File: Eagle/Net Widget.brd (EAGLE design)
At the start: 76.2 x 45.7 mm, 14 parts, among them IC1 ATmega1284P

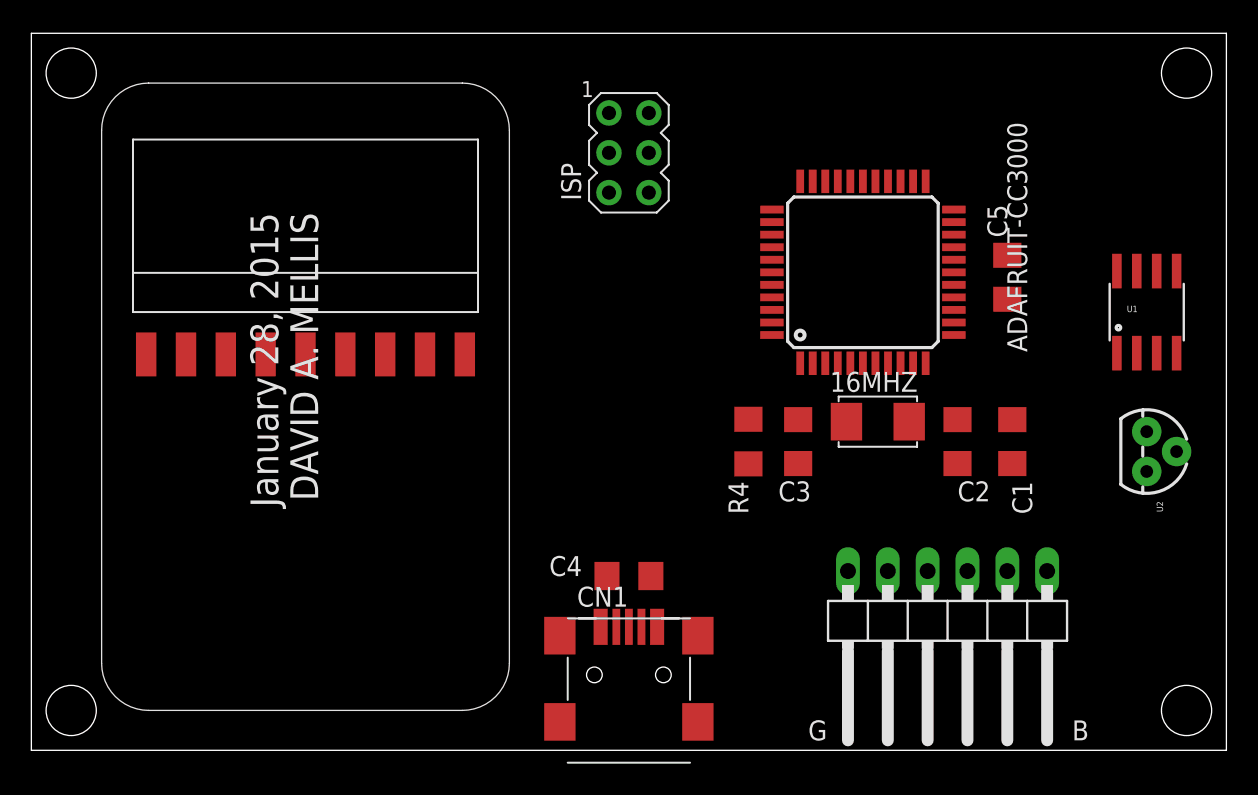
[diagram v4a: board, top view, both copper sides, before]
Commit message: Match CS and VBEN to Wicked Devices wildfire.
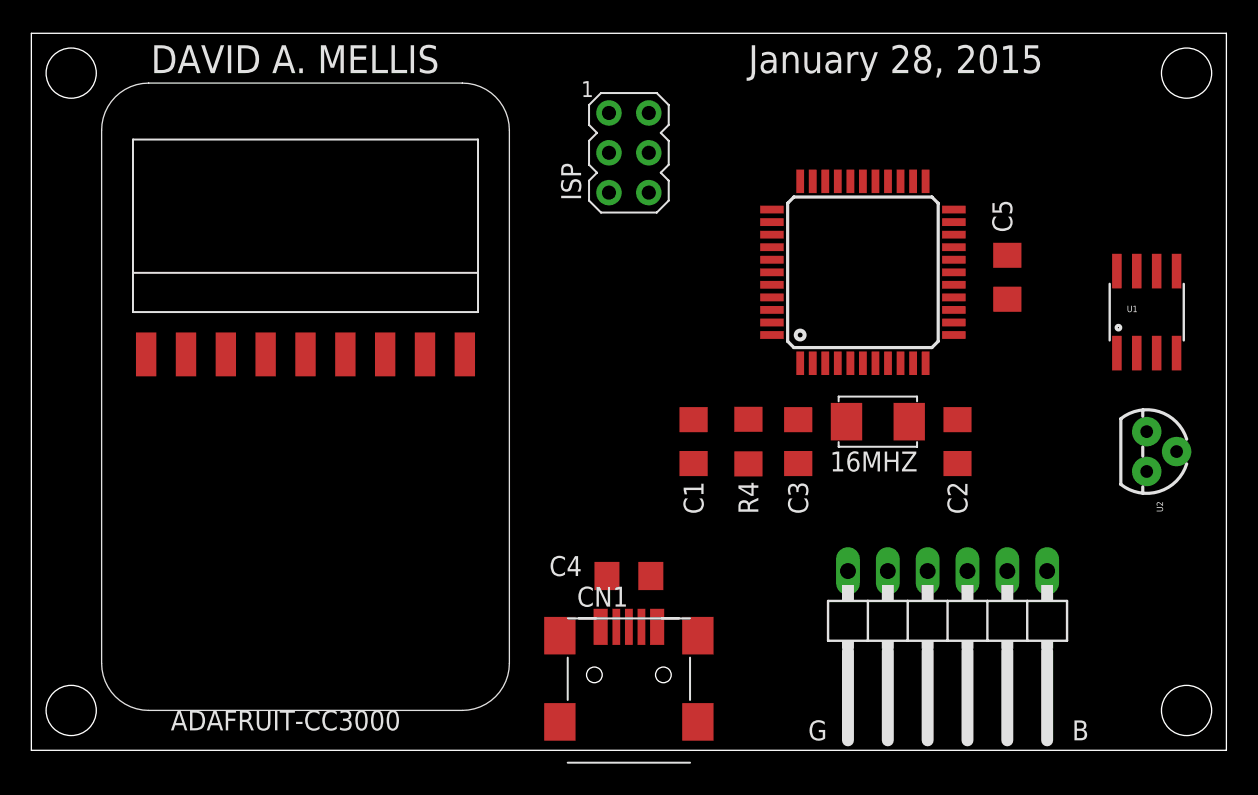
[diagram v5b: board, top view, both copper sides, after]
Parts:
- moved C1 20.3 mm to (42.2, 19.7)
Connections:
- net CS: now also IC1.40; no longer IC1.22
- net VBEN: now also IC1.41; no longer IC1.23
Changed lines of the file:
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@@
 <layer number="39" name="tKeepout" color="4" fill="11" visible="no" active="yes"/>
 <layer number="40" name="bKeepout" color="1" fill="11" visible="no" active="yes"/>
-<layer number="41" name="tRestrict" color="4" fill="10" visible="no" active="yes"/>
-<layer number="42" name="bRestrict" color="1" fill="10" visible="no" active="yes"/>
+<layer number="41" name="tRestrict" color="4" fill="10" visible="yes" active="yes"/>
+<layer number="42" name="bRestrict" color="1" fill="10" visible="yes" active="yes"/>
 <layer number="43" name="vRestrict" color="2" fill="10" visible="no" active="yes"/>
 <layer number="44" name="Drills" color="7" fill="1" visible="yes" active="yes"/>
@@
 <hole x="2.54" y="43.18" drill="3.2"/>
 <hole x="2.54" y="2.54" drill="3.2"/>
-<polygon width="0.4064" layer="41">
-<vertex x="37.465" y="20.32"/>
-<vertex x="38.735" y="20.32"/>
-<vertex x="41.275" y="22.86"/>
-<vertex x="41.275" y="25.4"/>
-<vertex x="46.355" y="25.4"/>
-<vertex x="46.355" y="24.13"/>
-<vertex x="44.45" y="24.13"/>
-<vertex x="44.45" y="15.24"/>
-<vertex x="46.355" y="15.24"/>
-<vertex x="46.355" y="13.97"/>
-<vertex x="41.275" y="13.97"/>
-<vertex x="41.275" y="16.51"/>
-<vertex x="39.37" y="18.415"/>
-<vertex x="37.465" y="18.415"/>
-</polygon>
-<text x="63.5" y="25.4" size="1.27" layer="25" font="fixed" rot="R90">ADAFRUIT-CC3000</text>
-<text x="16.51" y="34.29" size="1.778" layer="25" font="fixed" rot="R270">DAVID A. MELLIS</text>
-<text x="13.97" y="34.29" size="1.778" layer="25" font="fixed" rot="R270">January 28, 2015</text>
+<text x="8.89" y="1.27" size="1.27" layer="25" font="fixed">ADAFRUIT-CC3000</text>
+<text x="7.62" y="43.18" size="1.778" layer="25" font="fixed">DAVID A. MELLIS</text>
+<text x="45.72" y="43.18" size="1.778" layer="25" font="fixed">January 28, 2015</text>
 <text x="66.3575" y="0.635" size="1.27" layer="25" font="fixed" rot="SR0">B</text>
 <text x="49.53" y="0.635" size="1.27" layer="25" font="fixed" rot="SR0">G</text>
+<polygon width="0.4064" layer="42">
+<vertex x="48.26" y="17.78"/>
+<vertex x="59.69" y="17.78"/>
+<vertex x="59.69" y="22.86"/>
+<vertex x="54.61" y="22.86"/>
+<vertex x="54.61" y="25.4"/>
+<vertex x="53.6575" y="25.4"/>
+<vertex x="53.6575" y="22.86"/>
+<vertex x="48.26" y="22.86"/>
+</polygon>
 </plain>
 <attributes>
@@
 <elements>
 <element name="C2" library="rcl" package="C1206" value="18pF" x="59.055" y="19.685" smashed="yes" rot="R90">
-<attribute name="NAME" x="59.055" y="15.875" size="1.27" layer="25" font="fixed"/>
-<attribute name="VALUE" x="57.785" y="14.605" size="1.27" layer="27" font="fixed" rot="R90"/>
+<attribute name="NAME" x="58.42" y="17.145" size="1.27" layer="25" font="fixed" rot="R270"/>
+<attribute name="VALUE" x="61.2775" y="17.4625" size="1.27" layer="27" font="fixed" rot="R90"/>
 </element>
 <element name="C3" library="rcl" package="C1206" value="18pF" x="48.895" y="19.685" smashed="yes" rot="R90">
-<attribute name="NAME" x="47.625" y="15.875" size="1.27" layer="25" font="fixed"/>
-<attribute name="VALUE" x="51.435" y="14.605" size="1.27" layer="27" font="fixed" rot="R90"/>
+<attribute name="NAME" x="48.26" y="17.145" size="1.27" layer="25" font="fixed" rot="R270"/>
+<attribute name="VALUE" x="47.9425" y="17.4625" size="1.27" layer="27" font="fixed" rot="R90"/>
 </element>
 <element name="ISP" library="adafruit" package="AVRISP" value="AVRISP-6" x="38.1" y="38.1" smashed="yes">
@@
 </element>
 <element name="C5" library="rcl" package="C1206" value="0.1uF" x="62.23" y="30.1625" smashed="yes" rot="R90">
-<attribute name="NAME" x="62.23" y="32.7025" size="1.27" layer="25" font="fixed" rot="R90"/>
-<attribute name="VALUE" x="64.77" y="28.8925" size="1.27" layer="27" font="fixed" rot="R90"/>
+<attribute name="NAME" x="62.5475" y="33.02" size="1.27" layer="25" font="fixed" rot="R90"/>
+<attribute name="VALUE" x="64.4525" y="27.6225" size="1.27" layer="27" font="fixed" rot="R90"/>
 </element>
 <element name="16MHZ" library="Net Widget" package="2-SMD-5X3MM" value="CRYSTAL" x="53.975" y="20.955" smashed="yes" rot="R180">
-<attribute name="NAME" x="56.515" y="24.13" size="1.27" layer="25" font="fixed" rot="R180"/>
+<attribute name="NAME" x="56.515" y="19.05" size="1.27" layer="25" font="fixed" rot="R180"/>
 </element>
 <element name="R4" library="rcl" package="R1206" value="10K" x="45.72" y="19.685" smashed="yes" rot="R270">
-<attribute name="NAME" x="44.45" y="17.145" size="1.27" layer="25" rot="R270"/>
-<attribute name="VALUE" x="43.18" y="20.955" size="1.27" layer="27" rot="R270"/>
+<attribute name="NAME" x="45.085" y="17.145" size="1.27" layer="25" rot="R270"/>
+<attribute name="VALUE" x="43.4975" y="20.955" size="1.27" layer="27" rot="R270"/>
 </element>
 <element name="IC1" library="avr-5" package="TQFP44" value="ATmega1284P" x="53.0225" y="30.48" smashed="yes" rot="R90">
-<attribute name="VALUE" x="45.9026" y="25.0825" size="1.778" layer="27" rot="R90"/>
+<attribute name="VALUE" x="62.5475" y="39.5526" size="1.778" layer="27" rot="R180"/>
 </element>
 <element name="JP5" library="Net Widget" package="1X06/90" value="FTDI" x="58.42" y="7.62" smashed="yes" rot="R180">
 <attribute name="VALUE" x="66.675" y="8.89" size="1.27" layer="27" rot="SR270"/>
 </element>
-<element name="C1" library="rcl" package="C1206" value="0.1uF" x="62.5475" y="19.685" smashed="yes" rot="R270">
-<attribute name="NAME" x="62.5475" y="17.145" size="1.27" layer="25" rot="R270"/>
-<attribute name="VALUE" x="63.8175" y="22.225" size="1.27" layer="27" rot="R270"/>
+<element name="C1" library="rcl" package="C1206" value="0.1uF" x="42.2275" y="19.685" smashed="yes" rot="R270">
+<attribute name="NAME" x="41.5925" y="17.145" size="1.27" layer="25" rot="R270"/>
+<attribute name="VALUE" x="39.6875" y="22.225" size="1.27" layer="27" rot="R270"/>
 </element>
 <element name="CN1" library="Net Widget" package="USB-MINIB-POWER" value="" x="38.1" y="2.54"/>
@@
 <contactref element="R4" pad="1"/>
 <contactref element="C1" pad="1"/>
-<wire x1="51.4225" y1="24.68" x2="62.5475" y2="21.085" width="0" layer="19" extent="1-1"/>
 <wire x1="45.72" y1="21.107" x2="51.4225" y2="24.68" width="0" layer="19" extent="1-1"/>
-<wire x1="36.83" y1="35.56" x2="45.72" y2="21.107" width="0" layer="19" extent="1-1"/>
+<wire x1="42.2275" y1="21.085" x2="45.72" y2="21.107" width="0" layer="19" extent="1-1"/>
+<wire x1="36.83" y1="35.56" x2="42.2275" y2="21.085" width="0" layer="19" extent="1-1"/>
 </signal>
 <signal name="MOSI">
@@
 <signal name="CS">
 <contactref element="U$2" pad="P$7"/>
-<contactref element="IC1" pad="22"/>
-<wire x1="12.4" y1="25.245" x2="58.8225" y2="34.48" width="0" layer="19" extent="1-1"/>
+<contactref element="IC1" pad="40"/>
+<wire x1="12.4" y1="25.245" x2="47.2225" y2="29.68" width="0" layer="19" extent="1-1"/>
 </signal>
 <signal name="VBEN">
 <contactref element="U$2" pad="P$8"/>
-<contactref element="IC1" pad="23"/>
-<wire x1="9.86" y1="25.245" x2="57.0225" y2="36.28" width="0" layer="19" extent="1-1"/>
+<contactref element="IC1" pad="41"/>
+<wire x1="9.86" y1="25.245" x2="47.2225" y2="28.88" width="0" layer="19" extent="1-1"/>
 </signal>
 <signal name="IRQ">
@@
 <contactref element="JP5" pad="6"/>
 <contactref element="C1" pad="2"/>
-<wire x1="52.07" y1="11.43" x2="62.5475" y2="18.285" width="0" layer="19" extent="1-1"/>
+<wire x1="42.2275" y1="18.285" x2="52.07" y2="11.43" width="0" layer="19" extent="1-1"/>
 </signal>
 <signal name="RX">

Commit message: Auto-route board.
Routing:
- net VCC: track 0.00 -> 150.6 mm, vias 0 -> 3
- net GND: track 0.00 -> 141.6 mm, vias 0 -> 1
- net MOSI: track 0.00 -> 58.8 mm, vias 0 -> 1
- net MISO: track 0.00 -> 52.9 mm, vias 0 -> 2
- net SCK: track 0.00 -> 49.5 mm, vias 0 -> 2
- net CS: track 0.00 -> 43.2 mm
- net IRQ: track 0.00 -> 41.5 mm, vias 0 -> 2
- net VBEN: track 0.00 -> 39.7 mm, vias 0 -> 2
- net N$2: track 0.00 -> 32.3 mm, vias 0 -> 1
- net RESET: track 0.00 -> 27.9 mm
- net TX: track 0.00 -> 25.5 mm, vias 0 -> 1
- net N$1: track 0.00 -> 24.8 mm
- net RX: track 0.00 -> 18.4 mm
- net DTR: track 0.00 -> 12.7 mm
- net N$6: track 0.00 -> 7.64 mm
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
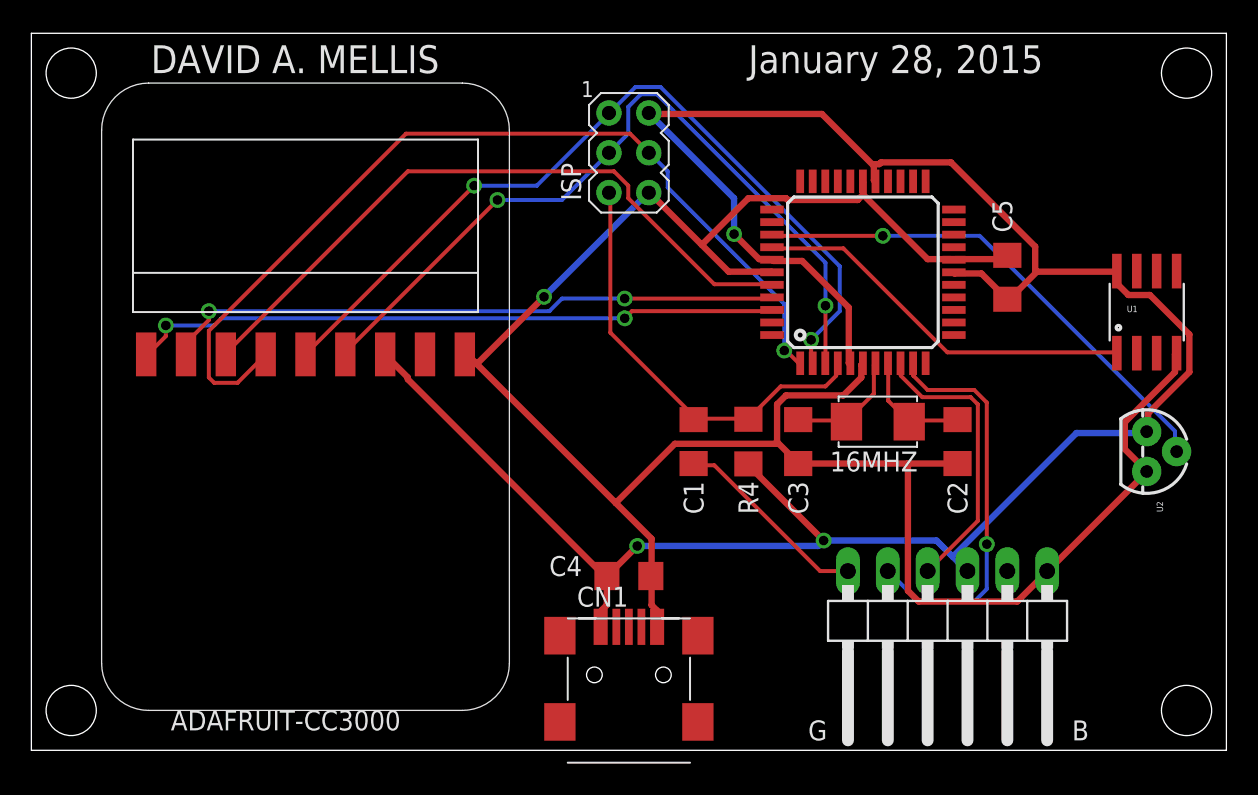
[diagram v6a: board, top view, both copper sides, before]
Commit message: Re-route w/ more space between pads and vias.
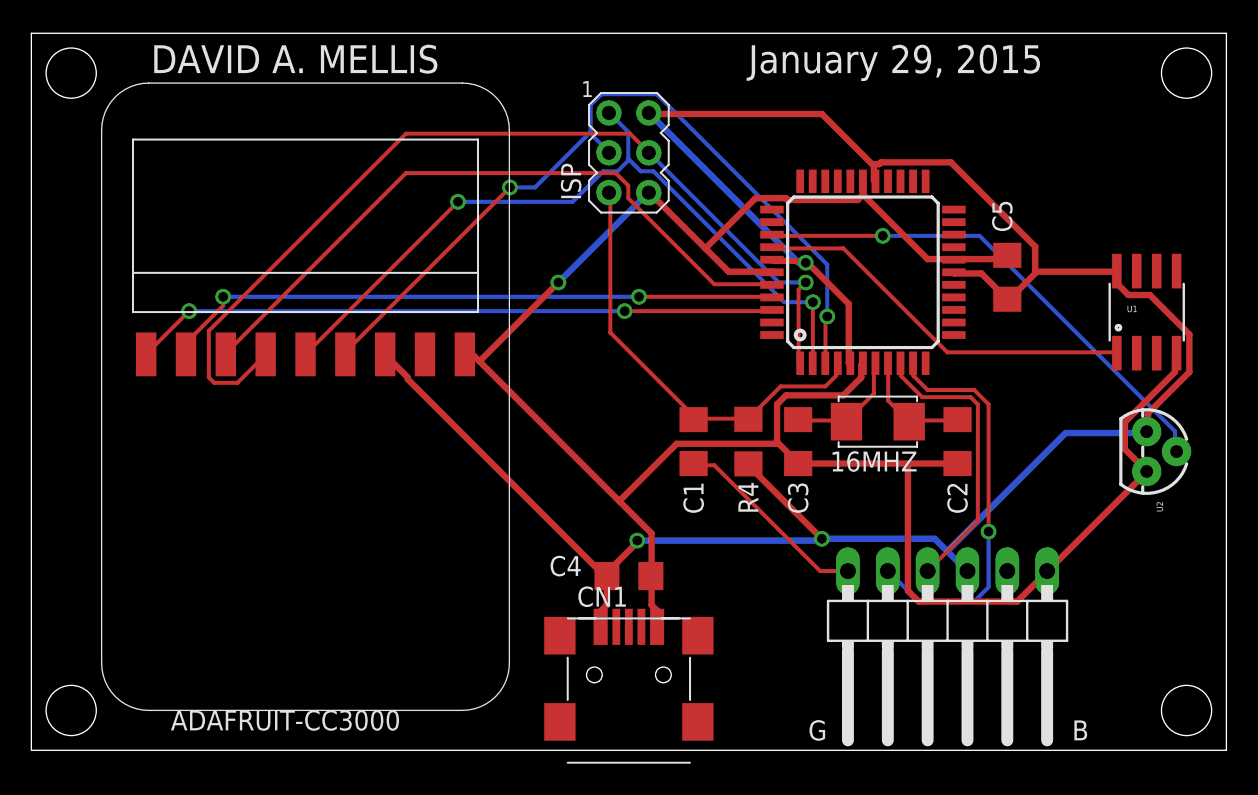
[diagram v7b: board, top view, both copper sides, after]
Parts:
- U1, U2: value (none) -> TMP36
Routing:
- net MISO: track 52.9 -> 48.7 mm
- net SCK: track 49.5 -> 51.3 mm
- net VCC: track 150.6 -> 152.1 mm
- net MOSI: track 58.8 -> 60.1 mm
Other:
- board text added: "January 29, 2015"
- board text removed: "January 28, 2015"

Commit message: Remove temp sensor; add LEDs and touch.
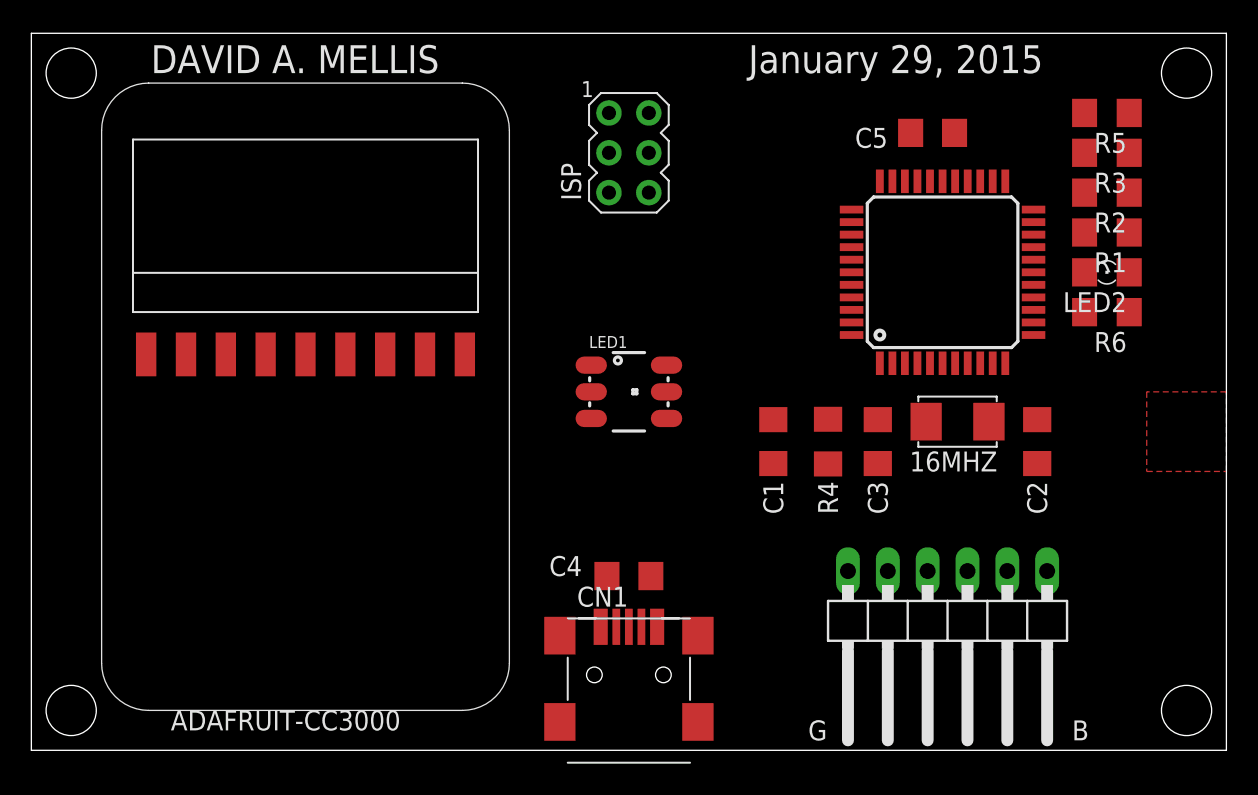
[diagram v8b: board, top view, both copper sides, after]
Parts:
- removed U1: TMP36, Net Widget:SO08
- removed U2: TMP36, Net Widget:TO-92
- added LED1: LED-TRICOLOR-5050NO_IC, SparkFun-LED:LED-TRICOLOR-5050
- added LED2: (no value), led:1206
- added R1, R2, R3, R5: 100, rcl:R1206
- added R6: 1M, rcl:R1206
- moved C5 10.4 mm to (57.5, 39.4), turned to 180 degrees
- moved C2 5.08 mm to (64.1, 19.7)
- moved 16MHZ 5.08 mm to (59.1, 21.0)
- moved C1 5.08 mm to (47.3, 19.7)
- moved C3 5.08 mm to (54.0, 19.7)
- moved IC1 5.08 mm to (58.1, 30.5)
- moved R4 5.08 mm to (50.8, 19.7)
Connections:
- removed net N$2: IC1.36, U2.2
- new net B: IC1.16, R5.2
- new net G: IC1.15, R3.2
- new net N$10: LED1.2, R2.1
- new net N$11: LED1.1, R3.1
- new net N$12: LED1.3, R5.1
- new net N$3: IC1.13, R1.2
- new net N$9: LED2.A, R1.1
- new net R: IC1.14, R2.2
- new net TOUCH: IC1.12, R6.1
- net GND: now also LED1.4, LED1.5, LED1.6, LED2.C; no longer U1.4, U2.3
- net N$1: now also IC1.11, R6.2; no longer IC1.37, U1.1
- net VCC: no longer U1.8, U2.1
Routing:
- net VCC: track 152.1 -> 0.00 mm, vias 3 -> 0
- net GND: track 141.2 -> 0.00 mm, vias 1 -> 0
- net MOSI: track 60.1 -> 0.00 mm, vias 1 -> 0
- net SCK: track 51.3 -> 0.00 mm, vias 2 -> 0
- net MISO: track 48.7 -> 0.00 mm, vias 2 -> 0
- net CS: track 43.1 -> 0.00 mm
- net IRQ: track 41.1 -> 0.00 mm, vias 2 -> 0
- net VBEN: track 39.7 -> 0.00 mm, vias 2 -> 0
- net N$2: track 32.3 -> 0.00 mm, vias 1 -> 0
- net RESET: track 27.9 -> 0.00 mm
- net TX: track 25.6 -> 0.00 mm, vias 1 -> 0
- net N$1: track 24.8 -> 0.00 mm
- net RX: track 18.4 -> 0.00 mm
- net DTR: track 12.7 -> 0.00 mm
- net N$6: track 7.64 -> 0.00 mm
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- added copper zone on layer 1, net TOUCH
